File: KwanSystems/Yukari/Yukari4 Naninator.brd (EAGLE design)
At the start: 43.2 x 17.8 mm, 43 parts, among them J001 USB_MICROB_JST, J501 GP-2106, J502 UP501, U001 FT232RLSSOP, U002 100nF, U003 100nF, U101 MPU-9250, U401 ATMEGA328P, U501 ADUM242E, U502 V_REG_LDOSMD2, U516 100nF, U521 100nF, U601 ADUM3221, Y401 16MHz

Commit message: More progress
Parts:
- removed C511: 0.1uF, SparkFun:0402-CAP
- removed C512, C552: 10uF, SparkFun:EIA3216
- removed C551: 1uF, SparkFun:0402-CAP
- removed FRAME1: FRAME-LETTER, SparkFun-Aesthetics:CREATIVE_COMMONS
- removed U$1: THR_SERVO_CONN, KwanSystems:THR_SERVO_CONN
- removed U$3: PI_CONN, KwanSystems:PI_CONN
- removed U002, U003: 100nF, SparkFun:0402-CAP
- removed U502: V_REG_LDOSMD2, SparkFun:SC70
- added C211, C221: 1uF, SparkFun:0402-CAP
- added C214, C224, C601, C608: 100nF, SparkFun:0402-CAP
- added C215, C225, C303, C304: 4.7uF, SparkFun:0402-CAP
- added D301: YELLOW, SparkFun:LED-0603
- added D302: PMEG2005CT, KwanSystems:SOT-23-3
- added J002: USB_MICROB_JST, KwanSystems:UB-MC5BR3-SD204-4S
- added J101: PI_CONN, KwanSystems:PI_CONN
- added J301: JST 2mm, SparkFun:JST-2-SMD
- added JP3: T, SparkFun-Connectors:1X03
- added R304: 1.5k, SparkFun:0402-RES
- added R305, R6: 10k, SparkFun:0402-RES
- added S2: B3U-1000P, KwanSystems:B3U-1000P
- added S201: AYZ0202, KwanSystems:AYZ0202
- added U$2: (no value), KwanSystems:AXES
- added U201: 3.3V, KwanSystems:SOT-23-5
- added U202: 1.8V, KwanSystems:SOT-23-5
- added U301: MCP73831, KwanSystems:SOT-23-5
- C110, C113: device SparkFun-Capacitors:0603-CAP -> SparkFun-Capacitors:0402-CAP
- JP5: value STEERING -> S
- moved U501 73.1 mm to (11.4, 31.5), turned to 270 degrees
- moved U521 72.3 mm to (5.08, 35.3), turned to 90 degrees
- moved U516 65.1 mm to (17.8, 35.3), turned to 90 degrees
- moved JP6 58.8 mm to (11.4, 1.27)
- moved JP7 48.2 mm to (19.1, 1.27)
- moved C113 42.4 mm to (20.6, 33.8), turned to 270 degrees
- moved C110 37.6 mm to (21.8, 33.8)
- moved U101 37.6 mm to (21.7, 37.9)
- moved C008 33.2 mm to (4.57, 22.9)
- moved JP5 26.7 mm to (36.8, 29.2)
- moved U601 11.7 mm to (31.0, 30.2), turned to 270 degrees
- moved C408 3.21 mm to (33.8, 14.5), turned to 0 degrees
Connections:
- removed net N$14: U501.2, U501.8, U521.1
- removed net N$15: U501.15, U501.9, U516.1
- new net BYP1.8: C224.1, U202.4
- new net BYP3.3: C214.1, U201.4
- new net GGND: C211.2, C214.2, C215.2, C221.2, C224.2, C225.2, C303.2, C304.2, J002.5, J002.P$10, J002.P$11, J002.P$6, J002.P$7, J002.P$8, J002.P$9, J301.1, R305.1, S201.1, S201.6, U201.2, U202.2, U301.2, U501.2, U501.8, U521.1
- new net N$10: R305.2, U301.5
- new net N$12: D301.C, U301.1
- new net N$13: D301.A, R304.1
- new net PWR_EN1.8: S201.5, U202.3
- new net PWR_EN3.3: S201.2, U201.3
- new net VBUS: C304.1, D302.1, J002.1, R304.2, U301.4
- new net VGPS: C008.A, C215.1, C225.1, J502.4, J502.5, U201.5, U202.5, U501.1, U521.2
- new net VIN: C211.1, C221.1, D302.3, S201.3, S201.4, U201.1, U202.1
- new net VLIPO: C303.1, D302.2, J301.2, U301.3
- net 1.8V: no longer C551.1, C552.A, U501.1, U502.5, U521.2
- net 3.3V: now also J101.3V3_1, J101.3V3_2, R6.2; no longer C511.1, C512.A, J502.4, J502.5, U$3.3V3_1, U$3.3V3_2, U502.1, U502.3
- net 5V: now also C601.2, J101.5V0_1, J101.5V0_2; no longer U$3.5V0_1, U$3.5V0_2, U002.2
- net GND: now also C008.C, C601.1, J101.GND_1, J101.GND_2, J101.GND_3, J101.GND_4, J101.GND_5, S2.P$2, U501.15, U501.9, U516.1; no longer C511.2, C512.C, C551.2, C552.C, U$3.GND_1, U$3.GND_2, U$3.GND_3, U$3.GND_4, U$3.GND_5, U002.1, U502.2
- net N$6: now also U601.6; no longer U601.7
- net N$7: now also JP3.3, U601.7; no longer U$1.SIGNAL, U601.6
- net ONOFF: now also R6.1, S2.P$1
- net PGND: now also C608.1, JP3.1; no longer U$1.GND, U$1.NC1, U$1.NC2, U$1.NC3, U$1.NC4, U$1.NC5, U003.1
- net PVCC: now also C608.2, JP3.2; no longer U$1.PWR, U003.2
- net RX_GPS: now also J101.TXD; no longer U$3.TXD
- net SCL: now also J101.SCL; no longer U$3.SCL
- net SDA: now also J101.SDA; no longer U$3.SDA
- net S_SERVO: now also U601.3; no longer U601.2
- net TX_GPS: now also J101.RXD; no longer U$3.RXD
- net T_SERVO: now also U601.2; no longer U601.3
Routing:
- net 5V: track 8.37 -> 129.6 mm
- net GGND: track 0.00 -> 80.8 mm
- net RX_GPS: track 0.00 -> 50.0 mm, vias 0 -> 1
- net TX_GPS: track 0.00 -> 48.7 mm, vias 0 -> 2
- net VGPS: track 0.00 -> 46.0 mm, vias 0 -> 2
- net 3.3V: track 0.00 -> 44.4 mm
- net VIN: track 0.00 -> 32.4 mm, vias 0 -> 3
- net D13: track 0.00 -> 30.4 mm
- net RESET: track 0.00 -> 23.5 mm
- net PPS: track 0.00 -> 23.2 mm, vias 0 -> 1
- net D11: track 0.00 -> 21.4 mm
- net D12: track 0.00 -> 21.1 mm, vias 0 -> 1
- net PVCC: track 0.00 -> 21.1 mm
- net SDA: track 0.00 -> 17.2 mm
- net SCL: track 0.00 -> 15.6 mm
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- added copper zone on layer 1, net GND
- added copper zone on layer 16, net GND
- added copper zone on layer 1, net PGND
- added copper zone on layer 16, net PGND
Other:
- board size 43.2 x 17.8 mm -> 43.2 x 56 mm
- board text added: "BLK"
- board text added: "GND"
- board text added: "PWR"
- board text added: "RED"
- board text added: "SIG"
- board text added: "WHT"
- board text removed: ">DESIGNER"
- board text removed: "ACCEL & GRYO"
- board text removed: "MAG"
- board text removed: "X"
- board text removed: "Y"
- board text removed: "Z"

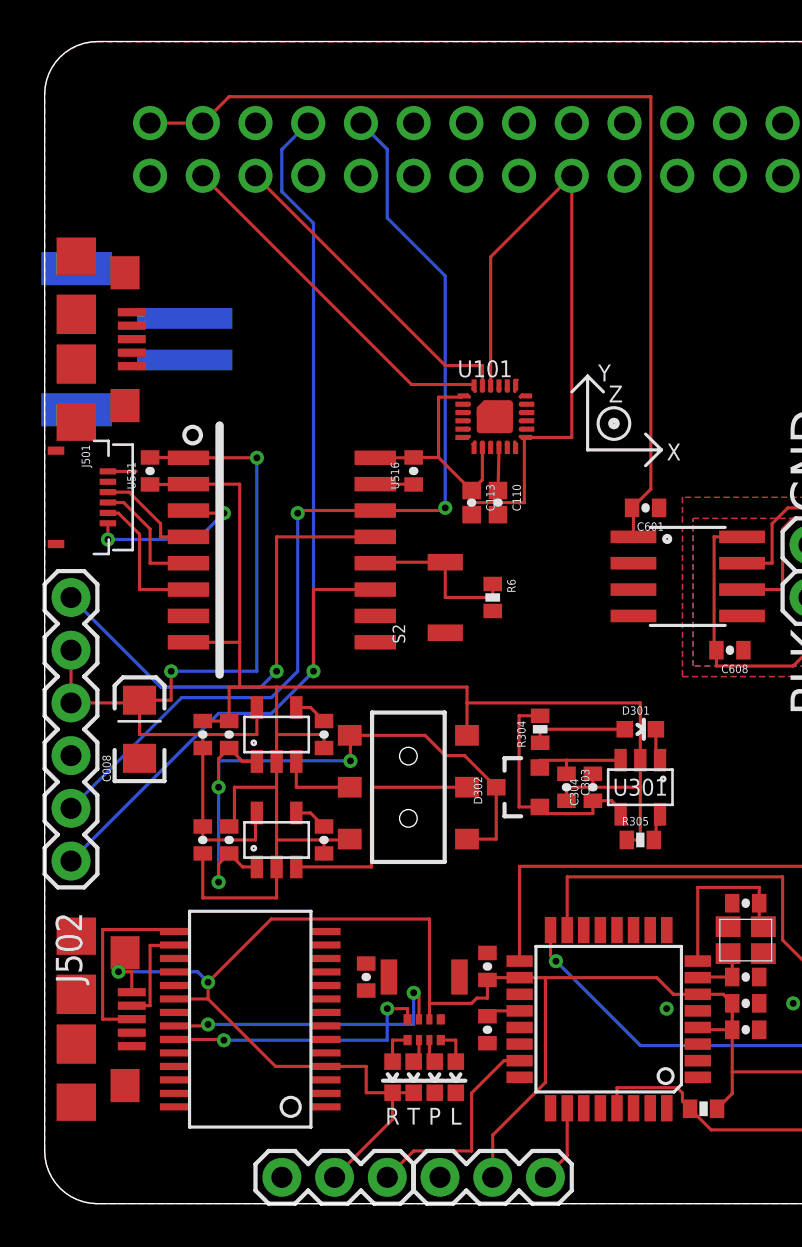
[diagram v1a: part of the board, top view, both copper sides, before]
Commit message: Added Adafruit stuff
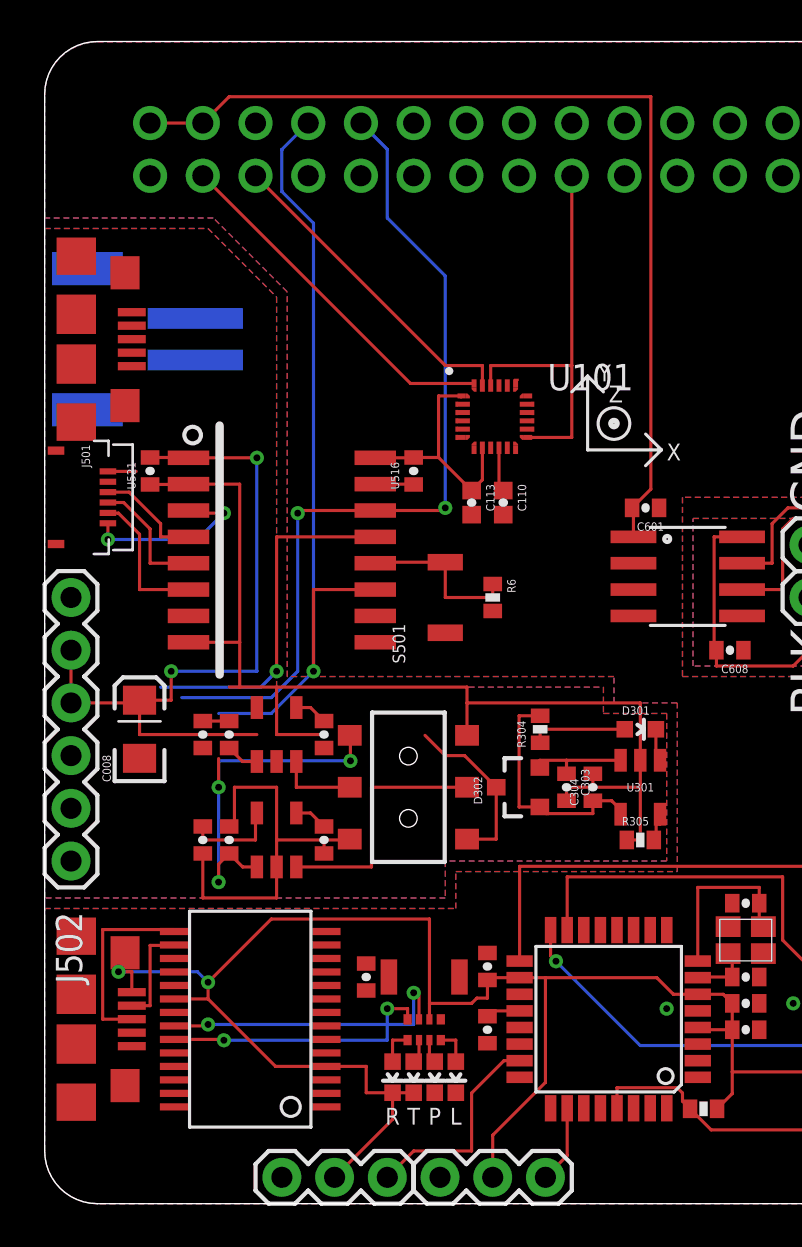
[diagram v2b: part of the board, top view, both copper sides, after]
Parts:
- C110, C113: value 0.1uF -> 100nF
- U101: value MPU-9250 -> MPU9250; device Testing:QFN24_PAD -> KwanSystems:LQFN_3MM_3MM
- moved J301 0.51 mm to (3.56, 41.7)
- moved C110 0.25 mm to (22.1, 33.8)
- renumbered J002 to J302, S2 to S501
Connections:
- net VIN renamed VIN_GPS
- removed net 1.8V: J501.VCC
- removed net AUX_CL: U101.7
- removed net AUX_DA: U101.21
- removed net FSYNC: U101.11
- new net TX_I: J502.2
- net 1PPS_I: now also J502.6
- net GND: no longer U101.CENTER
- net PPS: no longer J502.6
- net RX_GPS: no longer J502.1
- net RX_I: now also J502.1
- net TX_GPS: no longer J502.2
- net VGPS: now also J501.VCC
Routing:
- net 3.3V: track 44.4 -> 31.5 mm
- net RX_GPS: track 50.0 -> 39.9 mm
- net TX_GPS: track 48.7 -> 41.2 mm
- net PPS: track 23.2 -> 17.1 mm
- net GGND: track 80.8 -> 75.9 mm
- net VIN_GPS: track 32.4 -> 28.0 mm
- net VGPS: track 46.0 -> 41.6 mm
- net 1.8V: track 1.36 -> 0.00 mm
- added copper zone on layer 1, net GGND
- added copper zone on layer 16, net GGND
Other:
- board text removed: "All units in inch"
